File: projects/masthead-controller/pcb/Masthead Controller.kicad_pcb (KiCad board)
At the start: 4 copper layers, 150 x 83 mm, 220 parts, among them Q1 2N7002, Q2 2N7002, Q3 BSS138P,215, Q4 BSS138P,215, SW1 SW_MEC_5G, SW2 SW_MEC_5G

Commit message: Several v1.3.0 changes;
* CERN license corrected on PCB
* VR1's MODE/SYNC to R3 changed from +3.3V to new /VR1_vcc
* ROMs moved to sensor I2C bus
* New Config switch added (used to command DAC address config on power up if
  closed on boot)

Signed-off-by: digimer <digital.mermaid@gmail.com>
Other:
- board text added: "© Tuskar Marine - CERN-OHL-W-2.0"
- board text removed: "© Tuskar Marine - CERN OHL-WR v2"

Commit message: Updated the PCB to implement the updated schematics
Signed-off-by: digimer <digital.mermaid@gmail.com>
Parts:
- added C63: 0.1uF, mr-stuff:Kyocera AVX 0805, F.Cu at (76.6, 99.8)
- added R50: 10kR, mr-stuff:Stackpole RNCP0805, F.Cu at (74.5, 99.8)
- added R51: 475R, mr-stuff:Stackpole RNCP0805, F.Cu at (153.4, 91.2)
- added SW3: SW_MEC_5G, mr-stuff:SW_TS03-66-50-BK-160-LCR-D-67, F.Cu at (81.1, 100.8)
- moved C15 4.03 mm to (73.4, 107.4)
- moved R6 4.03 mm to (75.5, 107.4)
- moved C12 2.24 mm to (73.4, 94.4)
- moved R5 2.24 mm to (75.5, 94.4)
- moved SW1 1.92 mm to (68.9, 95.5), turned to -90 degrees
- moved SW2 1.39 mm to (68.9, 106.2), turned to -90 degrees
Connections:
- C11 pad 2: Net-(VR1-VCC) -> /VR1_VCC
- MCU1 pad 31: unconnected-(MCU1-IO38-Pad31) -> /CONFIG_SW
- R3 pad 1: +3.3V -> /VR1_VCC
- ROM1 pad 5: /DAC_SDA -> /I2C_SDA
- ROM1 pad 6: /DAC_SCL -> /I2C_SCL
- ROM2 pad 5: /DAC_SDA -> /I2C_SDA
- ROM2 pad 6: /DAC_SCL -> /I2C_SCL
- VR1 pad 8: Net-(VR1-VCC) -> /VR1_VCC
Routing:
- net Net-(C63-Pad1): track 0.00 -> 94.4 mm, vias 0 -> 1
- net /I2C_SDA: track 155.3 -> 180.2 mm, vias 5 -> 8
- net /I2C_SCL: track 156.4 -> 181.2 mm, vias 5 -> 8
- net GND: track 246.2 -> 259.8 mm
- net Net-(MCU1-IO0): track 87.1 -> 97.6 mm
- net /VR1_VCC: track 0.00 -> 9.18 mm
- net /DAC_SDA: track 93.5 -> 85.6 mm
- net /DAC_SCL: track 97.4 -> 90.3 mm
- net /CONFIG_SW: track 0.00 -> 5.81 mm
- net /EFUSE_LED_SHUTDOWN: track 143.6 -> 148.4 mm
- net /PGOOD_LED: track 142.6 -> 147.4 mm
- net /EFUSE_LED_FAULT: track 152.5 -> 157.3 mm
- net Net-(MCU1-EN): track 72.1 -> 76.5 mm
- net Net-(VR1-VCC): track 3.30 -> 0.00 mm
- net +3.3V: track 95.7 -> 99.0 mm, vias 26 -> 25
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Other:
- board text added: "Config"

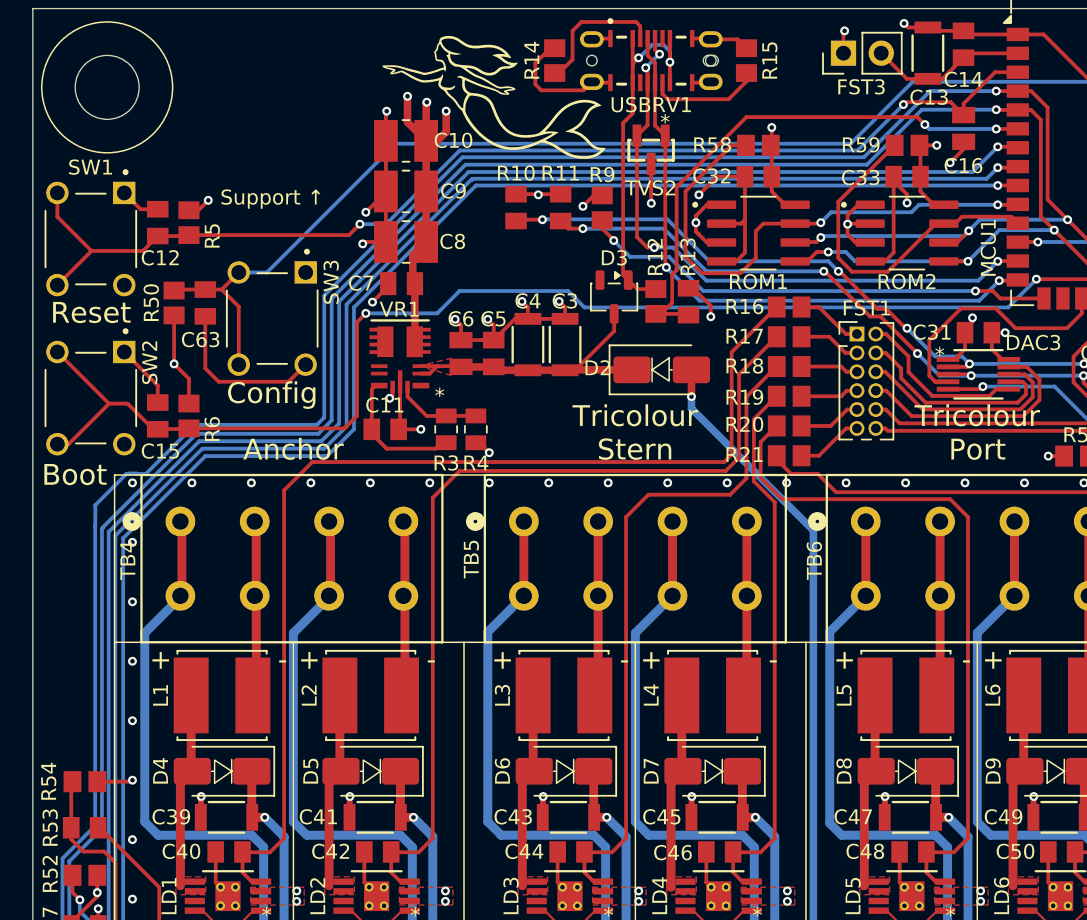
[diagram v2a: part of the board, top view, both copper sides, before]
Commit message: Added pull-up resistors to I2C_S{DA,CL}.
Signed-off-by: digimer <digital.mermaid@gmail.com>
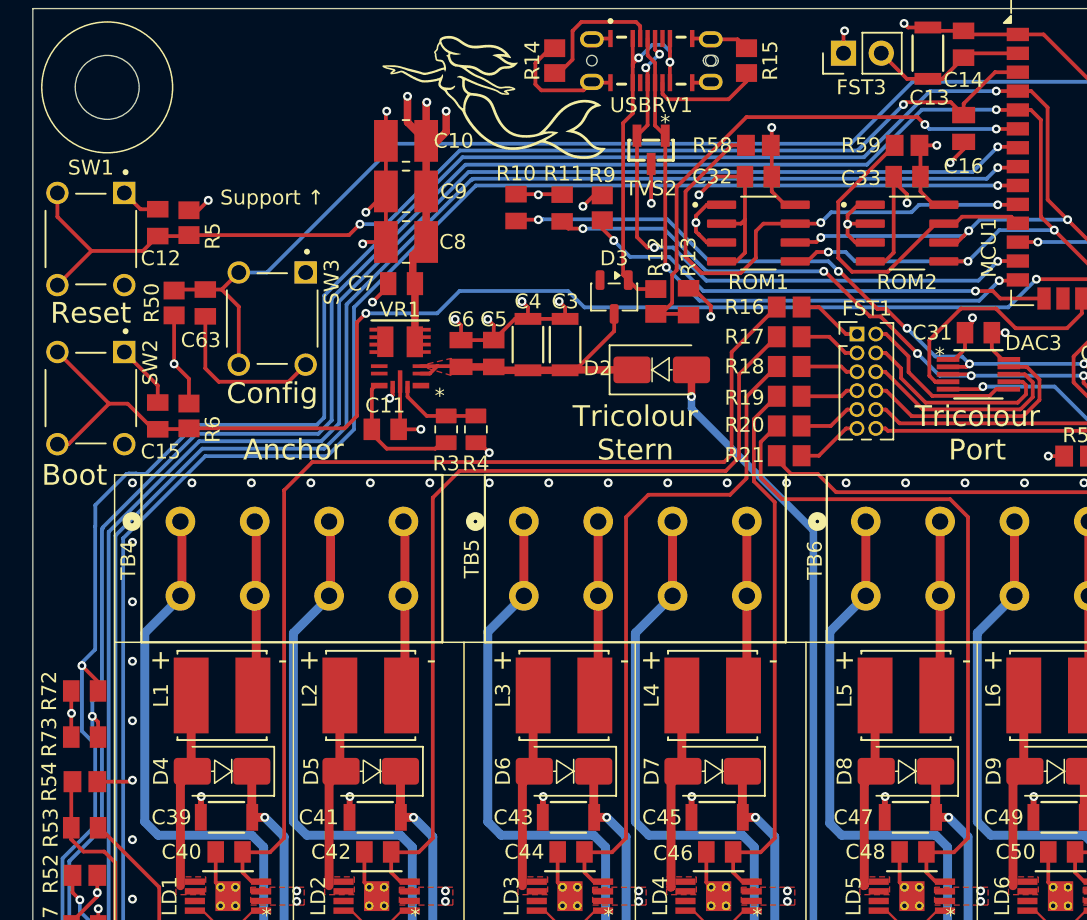
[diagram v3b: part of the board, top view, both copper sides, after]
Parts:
- added R72: 4.7kR, mr-stuff:Stackpole RMCA0805, F.Cu at (68.5, 125.9)
- added R73: 4.7kR, mr-stuff:Stackpole RMCA0805, F.Cu at (68.5, 129.0)
- moved R11 0.10 mm to (100.6, 93.4), turned to 90 degrees
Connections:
- R11 pad 1: +3.3V -> /DAC_SDA
- R11 pad 2: /DAC_SDA -> +3.3V
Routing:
- net +3.3V: track 99.0 -> 102.1 mm, vias 25 -> 26
- net /I2C_SCL: track 181.2 -> 184.1 mm, vias 8 -> 9
- net /I2C_SDA: track 180.2 -> 182.3 mm, vias 8 -> 9

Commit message: Standadized LEDs and GPIO resistors.
* Settled on 475 Ohm current limiting resistors for GPIO.
* Settled on Vishay TLMS1101-GS15 SMD LEDs.
* Added an LED to the Masthead controller for various status applications.

Signed-off-by: digimer <digital.mermaid@gmail.com>
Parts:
- added LED1: TLMS1101-GS15, mr-stuff:Vishay TLMS1101, F.Cu at (81.1, 95.0)
- added R75: 475R, mr-stuff:Stackpole RNCP0805, F.Cu at (83.6, 95.0)
- moved SW3 2.60 mm to (81.1, 103.5), turned to 90 degrees
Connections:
- MCU1 pad 30: unconnected-(MCU1-IO37-Pad30) -> /STATUS_LED
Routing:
- net /STATUS_LED: track 0.00 -> 77.0 mm, vias 0 -> 2
- net Net-(C63-Pad1): track 94.4 -> 98.5 mm
- net GND: track 259.8 -> 262.7 mm
- net Net-(LED1-A): track 0.00 -> 2.54 mm
- net Net-(MCU1-EN): track 76.5 -> 77.9 mm
- net /CAN_RX_LOCAL: track 27.7 -> 26.4 mm
- net /CAN_TX_LOCAL: track 40.4 -> 39.2 mm
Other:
- board text removed: "Support ↑"
